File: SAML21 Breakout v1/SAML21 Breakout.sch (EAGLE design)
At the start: 8 parts, among them U1 ATSAMD21JTQFP

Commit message: New parts
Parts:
- added C6, C7, C8: 10uF, dr-library:CAP0603
- added C9: 1uF, dr-library:CAP0603
- added R2: 330, dr-library:RESISTOR0603
- added S1: (no value), dr-library:SKHMQME010
- C1, C3, C4, C5: value 0.1uF -> 100nF
- C2: value 0.1uF -> 1uF
- U1: value ATSAMD21JTQFP -> AT-SAM-L21-JTQFP; device dr-library:ATSAMD21JTQFP -> dr-library:AT-SAM-L21-JTQFP
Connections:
- removed net N$2: R1.1, U1.RESET
- removed net N$7: C2.1, U1.VDDCORE
- new net N$3: C4.1, C7.1, L1.2, U1.VDDANA
- new net RESET: C9.1, R1.1, R2.2, U1.RESET
- net +3V3: now also C1.1, C2.1, C5.2, C6.1, C8.2, L1.1, U1.VDDCORE; no longer C4.1, C5.1, L1.2
- net GND: now also C5.1, C6.2, C7.2, C8.1, C9.2, S1.1, S1.3, U1.GND@22, U1.GND@33, U1.GND@47, U1.GND@54, U1.GNDANA; no longer C5.2
- net N$1: now also R2.1, S1.2; no longer C1.1, L1.1, U1.VDDANA
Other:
- moved on the sheet: C1, C2, C3, C4, C5, L1, R1, U1

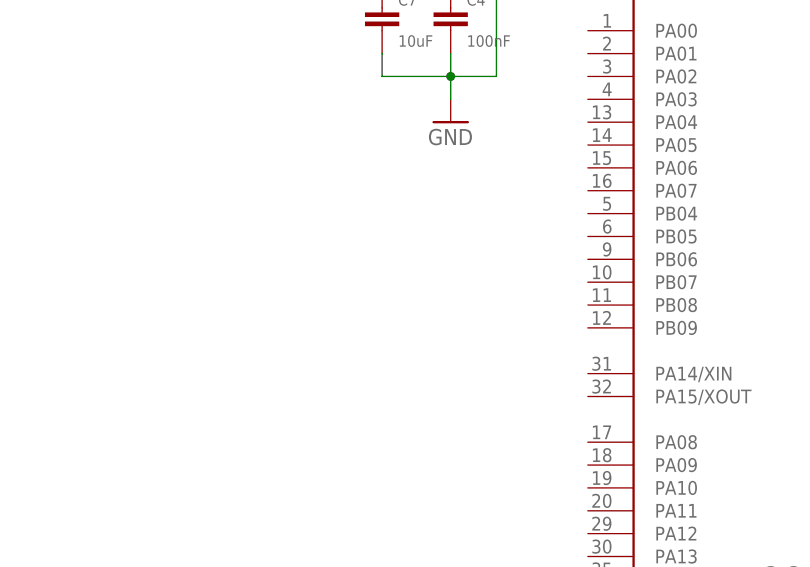
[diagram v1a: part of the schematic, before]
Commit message: Added crystal
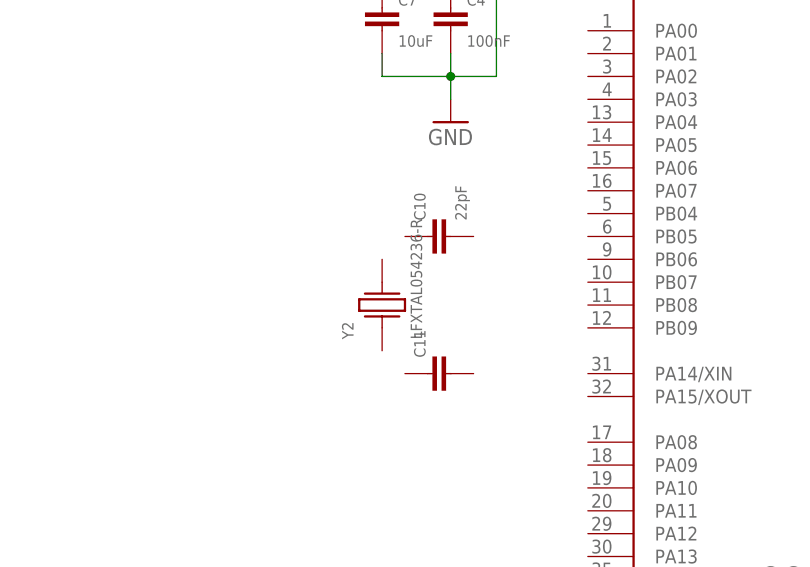
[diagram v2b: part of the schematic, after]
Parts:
- added C10: 22pF, dr-library:CAP0603
- added C11: (no value), dr-library:CAP0603
- added Y2: LFXTAL054236-R, dr-library:LFXTAL054236-R
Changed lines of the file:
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@@
 <part name="C9" library="dr-library" deviceset="CAP" device="0603" value="1uF"/>
 <part name="GND7" library="supply1" deviceset="GND" device=""/>
+<part name="C10" library="dr-library" deviceset="CAP" device="0603" value="22pF"/>
+<part name="C11" library="dr-library" deviceset="CAP" device="0603"/>
+<part name="Y2" library="dr-library" deviceset="LFXTAL054236-R" device=""/>
 </parts>
 <sheets>
@@
 <instance part="C9" gate="G$1" x="-58.42" y="58.42"/>
 <instance part="GND7" gate="1" x="-58.42" y="45.72"/>
+<instance part="C10" gate="G$1" x="-5.08" y="22.86" rot="R90"/>
+<instance part="C11" gate="G$1" x="-5.08" y="7.62" rot="R90"/>
+<instance part="Y2" gate="G$1" x="-12.7" y="15.24" rot="R90"/>
 </instances>
 <busses>

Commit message: More parts
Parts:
- added C12, C13: 4.7uF, dr-library:CAP0603
- added D1: (no value), dr-library:LED1206
- added J1: M50-4910545, dr-library:M50-4910545
- added R3: 330, dr-library:RESISTOR0603
- added U2: (no value), dr-library:AP7361C-33E-13
- C10: value 22pF -> 15pF
- C11: value (none) -> 15pF
- Y2: value LFXTAL054236-R -> 32.768MHz
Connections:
- new net N$2: D1.A, R3.1
- new net N$4: C10.2, U1.PA14/XIN, Y2.2
- new net N$5: C11.2, U1.PA15/XOUT, Y2.1
- new net SWCLK: J1.SWDCLK/TCK, U1.PA30
- new net SWDIO: J1.SWDIO/TMS, U1.PA31
- new net VCC: C12.1, U2.VIN
- net +3V3: now also C13.1, J1.VCC, R3.2, U2.VOUT
- net GND: now also C10.1, C11.1, C12.2, C13.2, D1.C, J1.GND@3, J1.GND@5, U2.GND
- net RESET: now also J1.RESET
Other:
- moved on the sheet: C10, C11, Y2
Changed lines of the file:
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@@
 <part name="C9" library="dr-library" deviceset="CAP" device="0603" value="1uF"/>
 <part name="GND7" library="supply1" deviceset="GND" device=""/>
-<part name="C10" library="dr-library" deviceset="CAP" device="0603" value="22pF"/>
-<part name="C11" library="dr-library" deviceset="CAP" device="0603"/>
-<part name="Y2" library="dr-library" deviceset="LFXTAL054236-R" device=""/>
+<part name="C10" library="dr-library" deviceset="CAP" device="0603" value="15pF"/>
+<part name="C11" library="dr-library" deviceset="CAP" device="0603" value="15pF"/>
+<part name="Y2" library="dr-library" deviceset="LFXTAL054236-R" device="" value="32.768MHz"/>
+<part name="GND8" library="supply1" deviceset="GND" device=""/>
+<part name="U2" library="dr-library" deviceset="AP7361C-33E-13" device=""/>
+<part name="C12" library="dr-library" deviceset="CAP" device="0603" value="4.7uF"/>
+<part name="C13" library="dr-library" deviceset="CAP" device="0603" value="4.7uF"/>
+<part name="P+1" library="supply1" deviceset="VCC" device=""/>
+<part name="+3V6" library="supply1" deviceset="+3V3" device=""/>
+<part name="GND9" library="supply1" deviceset="GND" device=""/>
+<part name="R3" library="dr-library" deviceset="RESISTOR" device="0603" value="330"/>
+<part name="D1" library="dr-library" deviceset="LED" device="1206"/>
+<part name="GND10" library="supply1" deviceset="GND" device=""/>
+<part name="J1" library="dr-library" deviceset="M50-4910545" device=""/>
+<part name="+3V7" library="supply1" deviceset="+3V3" device=""/>
+<part name="GND11" library="supply1" deviceset="GND" device=""/>
+<part name="+3V8" library="supply1" deviceset="+3V3" device=""/>
 </parts>
 <sheets>
@@
 <instance part="C9" gate="G$1" x="-58.42" y="58.42"/>
 <instance part="GND7" gate="1" x="-58.42" y="45.72"/>
-<instance part="C10" gate="G$1" x="-5.08" y="22.86" rot="R90"/>
-<instance part="C11" gate="G$1" x="-5.08" y="7.62" rot="R90"/>
-<instance part="Y2" gate="G$1" x="-12.7" y="15.24" rot="R90"/>
+<instance part="C10" gate="G$1" x="-12.7" y="12.7" rot="R90"/>
+<instance part="C11" gate="G$1" x="-12.7" y="-2.54" rot="R90"/>
+<instance part="Y2" gate="G$1" x="-7.62" y="5.08" rot="R90"/>
+<instance part="GND8" gate="1" x="-25.4" y="0"/>
+<instance part="U2" gate="G$1" x="109.22" y="91.44"/>
+<instance part="C12" gate="G$1" x="93.98" y="83.82"/>
+<instance part="C13" gate="G$1" x="124.46" y="83.82"/>
+<instance part="P+1" gate="VCC" x="93.98" y="101.6"/>
+<instance part="+3V6" gate="G$1" x="124.46" y="101.6"/>
+<instance part="GND9" gate="1" x="109.22" y="73.66"/>
+<instance part="R3" gate="G$1" x="81.28" y="91.44" rot="R90"/>
+<instance part="D1" gate="G$1" x="81.28" y="81.28" rot="R270"/>
+<instance part="GND10" gate="1" x="81.28" y="71.12"/>
+<instance part="J1" gate="G$1" x="116.84" y="48.26"/>
+<instance part="+3V7" gate="G$1" x="96.52" y="60.96"/>
+<instance part="GND11" gate="1" x="96.52" y="35.56"/>
+<instance part="+3V8" gate="G$1" x="81.28" y="101.6"/>
 </instances>
 <busses>
@@
 <junction x="-58.42" y="50.8"/>
 <pinref part="GND7" gate="1" pin="GND"/>
+</segment>
+<segment>
+<pinref part="C11" gate="G$1" pin="1"/>
+<wire x1="-17.78" y1="-2.54" x2="-20.32" y2="-2.54" width="0.1524" layer="91"/>
+<wire x1="-20.32" y1="-2.54" x2="-20.32" y2="5.08" width="0.1524" layer="91"/>
+<pinref part="C10" gate="G$1" pin="1"/>
+<wire x1="-20.32" y1="5.08" x2="-20.32" y2="12.7" width="0.1524" layer="91"/>
+<wire x1="-20.32" y1="12.7" x2="-17.78" y2="12.7" width="0.1524" layer="91"/>
+<pinref part="GND8" gate="1" pin="GND"/>
+<wire x1="-20.32" y1="5.08" x2="-25.4" y2="5.08" width="0.1524" layer="91"/>
+<wire x1="-25.4" y1="5.08" x2="-25.4" y2="2.54" width="0.1524" layer="91"/>
+<junction x="-20.32" y="5.08"/>
+</segment>
+<segment>
+<pinref part="C12" gate="G$1" pin="2"/>
+<wire x1="93.98" y1="81.28" x2="93.98" y2="78.74" width="0.1524" layer="91"/>
+<wire x1="93.98" y1="78.74" x2="109.22" y2="78.74" width="0.1524" layer="91"/>
+<pinref part="C13" gate="G$1" pin="2"/>
+<wire x1="109.22" y1="78.74" x2="124.46" y2="78.74" width="0.1524" layer="91"/>
+<wire x1="124.46" y1="78.74" x2="124.46" y2="81.28" width="0.1524" layer="91"/>
+<pinref part="U2" gate="G$1" pin="GND"/>
+<wire x1="109.22" y1="81.28" x2="109.22" y2="78.74" width="0.1524" layer="91"/>
+<junction x="109.22" y="78.74"/>
+<wire x1="109.22" y1="78.74" x2="109.22" y2="76.2" width="0.1524" layer="91"/>
+<pinref part="GND9" gate="1" pin="GND"/>
+</segment>
+<segment>
+<pinref part="GND10" gate="1" pin="GND"/>
+<pinref part="D1" gate="G$1" pin="C"/>
+<wire x1="81.28" y1="73.66" x2="81.28" y2="76.2" width="0.1524" layer="91"/>
+</segment>
+<segment>
+<pinref part="J1" gate="G$1" pin="GND@3"/>
+<wire x1="101.6" y1="50.8" x2="96.52" y2="50.8" width="0.1524" layer="91"/>
+<pinref part="J1" gate="G$1" pin="GND@5"/>
+<wire x1="101.6" y1="48.26" x2="96.52" y2="48.26" width="0.1524" layer="91"/>
+<wire x1="96.52" y1="50.8" x2="96.52" y2="48.26" width="0.1524" layer="91"/>
+<pinref part="GND11" gate="1" pin="GND"/>
+<wire x1="96.52" y1="48.26" x2="96.52" y2="38.1" width="0.1524" layer="91"/>
+<junction x="96.52" y="48.26"/>
 </segment>
 </net>
@@
 <wire x1="-58.42" y1="81.28" x2="-58.42" y2="78.74" width="0.1524" layer="91"/>
 </segment>
+<segment>
+<pinref part="+3V6" gate="G$1" pin="+3V3"/>
+<pinref part="C13" gate="G$1" pin="1"/>
+<wire x1="124.46" y1="99.06" x2="124.46" y2="93.98" width="0.1524" layer="91"/>
+<pinref part="U2" gate="G$1" pin="VOUT"/>
+<wire x1="124.46" y1="93.98" x2="124.46" y2="88.9" width="0.1524" layer="91"/>
+<wire x1="121.92" y1="93.98" x2="124.46" y2="93.98" width="0.1524" layer="91"/>
+<junction x="124.46" y="93.98"/>
+</segment>
+<segment>
+<pinref part="J1" gate="G$1" pin="VCC"/>
+<wire x1="101.6" y1="53.34" x2="96.52" y2="53.34" width="0.1524" layer="91"/>
+<pinref part="+3V7" gate="G$1" pin="+3V3"/>
+<wire x1="96.52" y1="53.34" x2="96.52" y2="58.42" width="0.1524" layer="91"/>
+</segment>
+<segment>
+<pinref part="R3" gate="G$1" pin="2"/>
+<wire x1="81.28" y1="96.52" x2="81.28" y2="99.06" width="0.1524" layer="91"/>
+<pinref part="+3V8" gate="G$1" pin="+3V3"/>
+</segment>
 </net>
 <net name="N$1" class="0">
@@
 <label x="2.54" y="58.42" size="1.778" layer="95"/>
 </segment>
-</net>
+<segment>
+<pinref part="J1" gate="G$1" pin="RESET"/>
+<wire x1="132.08" y1="43.18" x2="142.24" y2="43.18" width="0.1524" layer="91"/>
+<label x="134.62" y="43.18" size="1.778" layer="95"/>
+</segment>
+</net>
+<net name="N$4" class="0">
+<segment>
+<pinref part="C10" gate="G$1" pin="2"/>
+<wire x1="-10.16" y1="12.7" x2="-7.62" y2="12.7" width="0.1524" layer="91"/>
+<pinref part="Y2" gate="G$1" pin="2"/>
+<wire x1="-7.62" y1="12.7" x2="-7.62" y2="10.16" width="0.1524" layer="91"/>
+<pinref part="U1" gate="G$1" pin="PA14/XIN"/>
+<wire x1="10.16" y1="7.62" x2="-2.54" y2="7.62" width="0.1524" layer="91"/>
+<wire x1="-2.54" y1="7.62" x2="-2.54" y2="12.7" width="0.1524" layer="91"/>
+<wire x1="-2.54" y1="12.7" x2="-7.62" y2="12.7" width="0.1524" layer="91"/>
+<junction x="-7.62" y="12.7"/>
+</segment>
+</net>
+<net name="N$5" class="0">
+<segment>
+<pinref part="C11" gate="G$1" pin="2"/>
+<wire x1="-10.16" y1="-2.54" x2="-7.62" y2="-2.54" width="0.1524" layer="91"/>
+<pinref part="Y2" gate="G$1" pin="1"/>
+<wire x1="-7.62" y1="-2.54" x2="-7.62" y2="0" width="0.1524" layer="91"/>
+<wire x1="-7.62" y1="-2.54" x2="-2.54" y2="-2.54" width="0.1524" layer="91"/>
+<junction x="-7.62" y="-2.54"/>
+<wire x1="-2.54" y1="-2.54" x2="-2.54" y2="5.08" width="0.1524" layer="91"/>
+<pinref part="U1" gate="G$1" pin="PA15/XOUT"/>
+<wire x1="-2.54" y1="5.08" x2="10.16" y2="5.08" width="0.1524" layer="91"/>
+</segment>
+</net>
+<net name="VCC" class="0">
+<segment>
+<pinref part="P+1" gate="VCC" pin="VCC"/>
+<pinref part="C12" gate="G$1" pin="1"/>
+<wire x1="93.98" y1="99.06" x2="93.98" y2="93.98" width="0.1524" layer="91"/>
+<pinref part="U2" gate="G$1" pin="VIN"/>
+<wire x1="93.98" y1="93.98" x2="93.98" y2="88.9" width="0.1524" layer="91"/>
+<wire x1="96.52" y1="93.98" x2="93.98" y2="93.98" width="0.1524" layer="91"/>
+<junction x="93.98" y="93.98"/>
+</segment>
+</net>
+<net name="SWCLK" class="0">
+<segment>
+<pinref part="U1" gate="G$1" pin="PA30"/>
+<wire x1="60.96" y1="27.94" x2="71.12" y2="27.94" width="0.1524" layer="91"/>
+<label x="63.5" y="27.94" size="1.778" layer="95"/>
+</segment>
+<segment>
+<pinref part="J1" gate="G$1" pin="SWDCLK/TCK"/>
+<wire x1="132.08" y1="50.8" x2="142.24" y2="50.8" width="0.1524" layer="91"/>
+<label x="134.62" y="50.8" size="1.778" layer="95"/>
+</segment>
+</net>
+<net name="SWDIO" class="0">
+<segment>
+<pinref part="U1" gate="G$1" pin="PA31"/>
+<wire x1="60.96" y1="25.4" x2="71.12" y2="25.4" width="0.1524" layer="91"/>
+<label x="63.5" y="25.4" size="1.778" layer="95"/>
+</segment>
+<segment>
+<pinref part="J1" gate="G$1" pin="SWDIO/TMS"/>
+<wire x1="132.08" y1="53.34" x2="142.24" y2="53.34" width="0.1524" layer="91"/>
+<label x="134.62" y="53.34" size="1.778" layer="95"/>
+</segment>
+</net>
+<net name="N$2" class="0">
+<segment>
+<pinref part="D1" gate="G$1" pin="A"/>
+<pinref part="R3" gate="G$1" pin="1"/>
+<wire x1="81.28" y1="83.82" x2="81.28" y2="86.36" width="0.1524" layer="91"/>
+</segment>
+</net>

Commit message: Some changes
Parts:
- D1: value (none) -> PWR
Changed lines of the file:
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@@
 <part name="GND9" library="supply1" deviceset="GND" device=""/>
 <part name="R3" library="dr-library" deviceset="RESISTOR" device="0603" value="330"/>
-<part name="D1" library="dr-library" deviceset="LED" device="1206"/>
+<part name="D1" library="dr-library" deviceset="LED" device="1206" value="PWR"/>
 <part name="GND10" library="supply1" deviceset="GND" device=""/>
 <part name="J1" library="dr-library" deviceset="M50-4910545" device=""/>

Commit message: SAML21
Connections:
- new net 2.5V: U1.PA03
- net GND: now also J1.GNDDET
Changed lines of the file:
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@@
 <wire x1="96.52" y1="50.8" x2="96.52" y2="48.26" width="0.1524" layer="91"/>
 <pinref part="GND11" gate="1" pin="GND"/>
-<wire x1="96.52" y1="48.26" x2="96.52" y2="38.1" width="0.1524" layer="91"/>
+<wire x1="96.52" y1="48.26" x2="96.52" y2="43.18" width="0.1524" layer="91"/>
 <junction x="96.52" y="48.26"/>
+<pinref part="J1" gate="G$1" pin="GNDDET"/>
+<wire x1="96.52" y1="43.18" x2="96.52" y2="38.1" width="0.1524" layer="91"/>
+<wire x1="101.6" y1="43.18" x2="96.52" y2="43.18" width="0.1524" layer="91"/>
+<junction x="96.52" y="43.18"/>
 </segment>
 </net>
@@
 </segment>
 </net>
+<net name="2.5V" class="0">
+<segment>
+<pinref part="U1" gate="G$1" pin="PA03"/>
+<wire x1="10.16" y1="38.1" x2="2.54" y2="38.1" width="0.1524" layer="91"/>
+<label x="2.54" y="38.1" size="1.778" layer="95"/>
+</segment>
+</net>

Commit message: change
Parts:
- U2: value (none) -> AP7361C-33E-13
